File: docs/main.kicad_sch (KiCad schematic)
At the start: 7 parts, among them Q1 IRLB8743

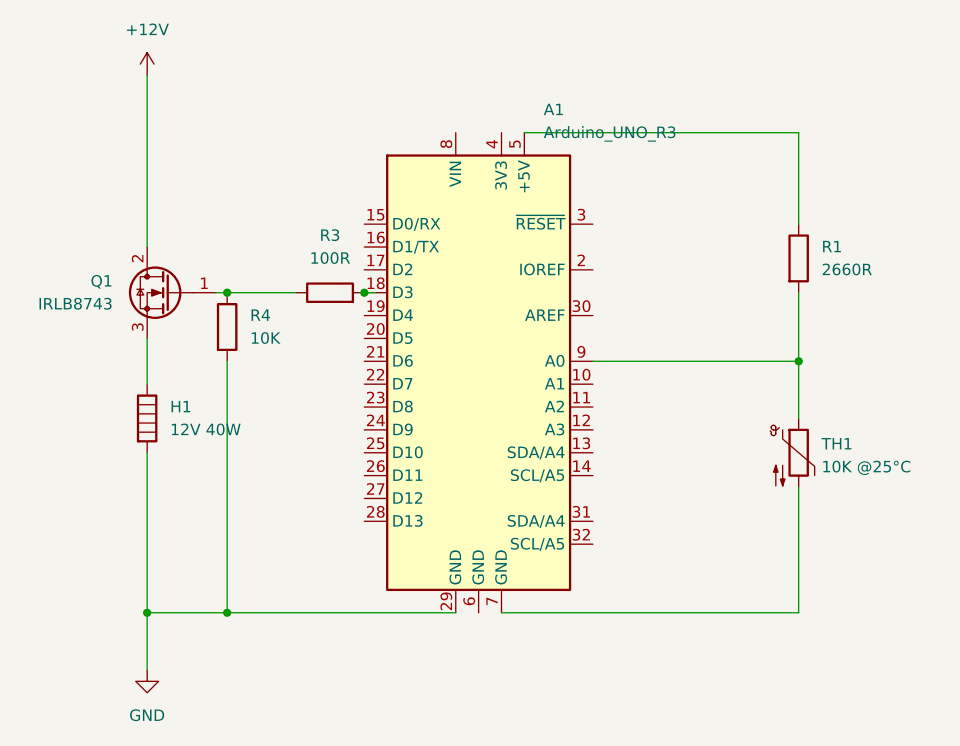
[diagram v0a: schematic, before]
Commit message: edit components & main circuit
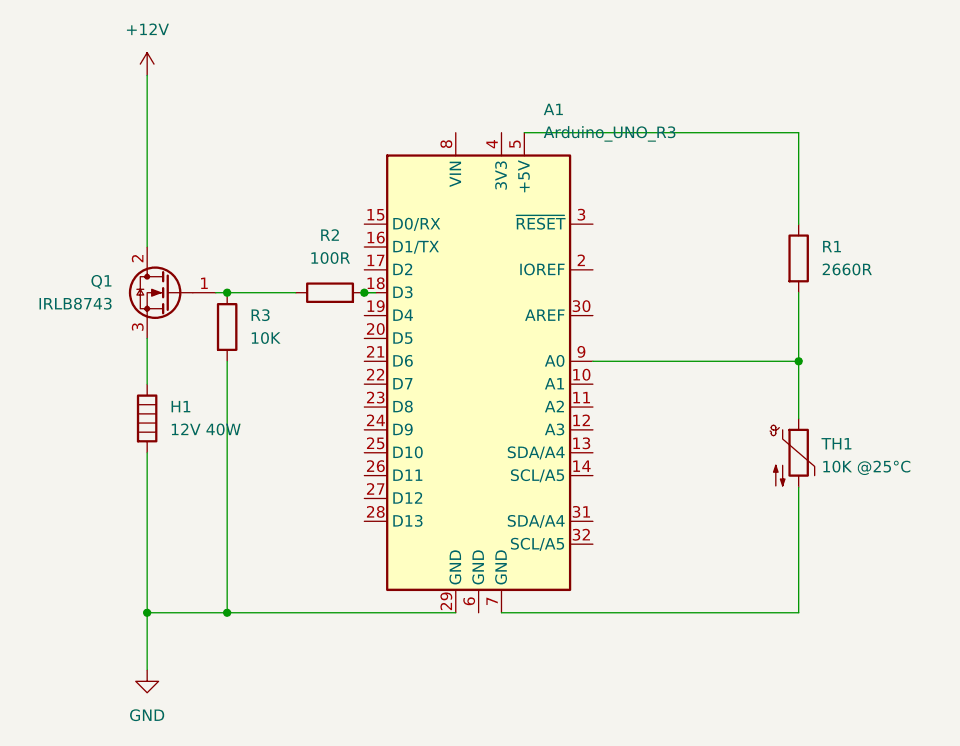
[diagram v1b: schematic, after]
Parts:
- renumbered R3 to R2, R4 to R3
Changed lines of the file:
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@@
 		(title "pid-temperature-controller|main")
 		(date "2026-05-13")
-		(rev "v1.0")
+		(rev "v1.1")
 	)
 	(junction
@@
 		(dnp no)
 		(fields_autoplaced yes)
-		(property "Reference" "R3"
+		(property "Reference" "R2"
 			(at 104.14 67.31 90)
 			(show_name no)
@@
 			(project "main"
 				(path "/65a569c9-b81d-4fcf-906a-443098e8f4b2"
-					(reference "R3")
+					(reference "R2")
 					(unit 1)
 				)
@@
 		(dnp no)
 		(fields_autoplaced yes)
-		(property "Reference" "R4"
+		(property "Reference" "R3"
 			(at 95.25 76.1999 0)
 			(show_name no)
@@
 			(project "main"
 				(path "/65a569c9-b81d-4fcf-906a-443098e8f4b2"
-					(reference "R4")
+					(reference "R3")
 					(unit 1)
 				)

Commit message: updated hardware
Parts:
- added C1: 100nF, symbol Device:C
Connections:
- net at R1.2, TH1.1: now also C1.2; no longer A1.9 (A0)
- new net: A1.9 (A0), C1.1
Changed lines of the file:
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@@
 		(title "pid-temperature-controller|main")
 		(date "2026-05-13")
-		(rev "v1.1")
+		(rev "v1.2")
 	)
 	(junction
@@
 	(wire
 		(pts
-			(xy 133.35 81.28) (xy 156.21 81.28)
-		)
-		(stroke
-			(width 0)
-			(type default)
-		)
-	)
-	(wire
-		(pts
 			(xy 83.82 49.53) (xy 83.82 68.58)
 		)
@@
 	(wire
 		(pts
+			(xy 133.35 81.28) (xy 134.62 81.28)
+		)
+		(stroke
+			(width 0)
+			(type default)
+		)
+	)
+	(wire
+		(pts
 			(xy 92.71 81.28) (xy 92.71 109.22)
 		)
@@
 	(wire
 		(pts
+			(xy 142.24 81.28) (xy 156.21 81.28)
+		)
+		(stroke
+			(width 0)
+			(type default)
+		)
+	)
+	(wire
+		(pts
 			(xy 156.21 73.66) (xy 156.21 81.28)
 		)
@@
 	(wire
 		(pts
+			(xy 83.82 109.22) (xy 92.71 109.22)
+		)
+		(stroke
+			(width 0)
+			(type default)
+		)
+	)
+	(wire
+		(pts
+			(xy 83.82 91.44) (xy 83.82 109.22)
+		)
+		(stroke
+			(width 0)
+			(type default)
+		)
+	)
+	(wire
+		(pts
+			(xy 83.82 109.22) (xy 83.82 115.57)
+		)
+		(stroke
+			(width 0)
+			(type default)
+		)
+	)
+	(wire
+		(pts
+			(xy 92.71 73.66) (xy 100.33 73.66)
+		)
+		(stroke
+			(width 0)
+			(type default)
+		)
+	)
+	(wire
+		(pts
+			(xy 83.82 78.74) (xy 83.82 83.82)
+		)
+		(stroke
+			(width 0)
+			(type default)
+		)
+	)
+	(wire
+		(pts
+			(xy 125.73 55.88) (xy 156.21 55.88)
+		)
+		(stroke
+			(width 0)
+			(type default)
+		)
+	)
+	(wire
+		(pts
 			(xy 156.21 81.28) (xy 156.21 87.63)
-		)
-		(stroke
-			(width 0)
-			(type default)
-		)
-	)
-	(wire
-		(pts
-			(xy 83.82 109.22) (xy 92.71 109.22)
-		)
-		(stroke
-			(width 0)
-			(type default)
-		)
-	)
-	(wire
-		(pts
-			(xy 83.82 91.44) (xy 83.82 109.22)
-		)
-		(stroke
-			(width 0)
-			(type default)
-		)
-	)
-	(wire
-		(pts
-			(xy 83.82 109.22) (xy 83.82 115.57)
-		)
-		(stroke
-			(width 0)
-			(type default)
-		)
-	)
-	(wire
-		(pts
-			(xy 92.71 73.66) (xy 100.33 73.66)
-		)
-		(stroke
-			(width 0)
-			(type default)
-		)
-	)
-	(wire
-		(pts
-			(xy 83.82 78.74) (xy 83.82 83.82)
-		)
-		(stroke
-			(width 0)
-			(type default)
-		)
-	)
-	(wire
-		(pts
-			(xy 125.73 55.88) (xy 156.21 55.88)
 		)
 		(stroke
@@
 					(unit 1)
 				)
+			)
+		)
+	)
+	(symbol
+		(lib_id "Device:C")
+		(at 138.43 81.28 90)
+		(unit 1)
+		(body_style 1)
+		(exclude_from_sim no)
+		(in_bom yes)
+		(on_board yes)
+		(in_pos_files yes)
+		(dnp no)
+		(fields_autoplaced yes)
+		(property "Reference" "C1"
+			(at 137.1599 77.47 0)
+			(show_name no)
+			(do_not_autoplace no)
+			(effects
+				(font
+					(size 1.27 1.27)
+				)
+				(justify left)
+			)
+		)
+		(property "Value" "100nF"
+			(at 139.6999 77.47 0)
+			(show_name no)
+			(do_not_autoplace no)
+			(effects
+				(font
+					(size 1.27 1.27)
+				)
+				(justify left)
+			)
+		)
+		(property "Footprint" ""
+			(at 142.24 80.3148 0)
+			(hide yes)
+			(show_name no)
+			(do_not_autoplace no)
+			(effects
+				(font
+					(size 1.27 1.27)
+				)
+			)
+		)
+		(property "Datasheet" ""
+			(at 138.43 81.28 0)
+			(hide yes)
+			(show_name no)
+			(do_not_autoplace no)
+			(effects
+				(font
+					(size 1.27 1.27)
+				)
+			)
+		)
+		(property "Description" "Unpolarized capacitor"
+			(at 138.43 81.28 0)
+			(hide yes)
+			(show_name no)
+			(do_not_autoplace no)
+			(effects
+				(font
+					(size 1.27 1.27)
+				)
+			)
+		)
+		(pin "2"
+		)
+		(pin "1"
+		)
+		(instances
+			(project "main"
+				(path "/65a569c9-b81d-4fcf-906a-443098e8f4b2"
+					(reference "C1")
+					(unit 1)
+				)
